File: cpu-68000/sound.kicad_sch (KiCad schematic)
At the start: 40 parts, among them U601 74HCT2G04, U602 SAA1099, U603 SAA1099, U604 LDL1117S50R, Y601 7.15909MHz

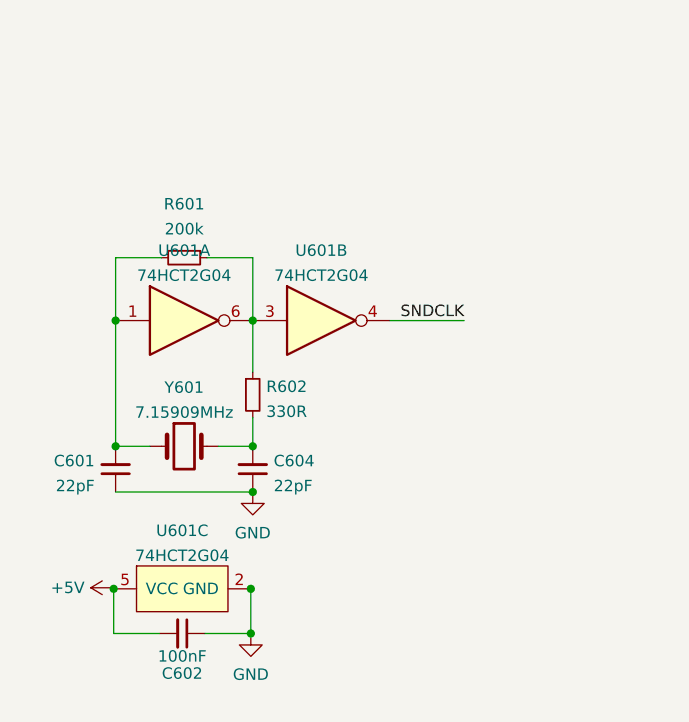
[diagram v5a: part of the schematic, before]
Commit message: Minor cleanup of CPU board
- Switched out of stock 2 bit level shifters for 8 bit part we already
  have; this means that the function codes will be buffered along with
  all other signals.
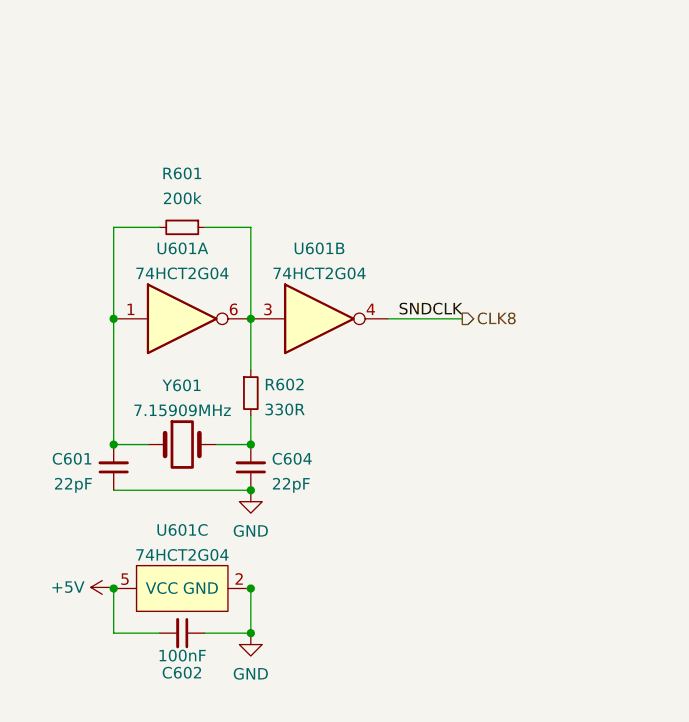
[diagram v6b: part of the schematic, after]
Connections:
- net SNDCLK renamed CLK8
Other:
- moved on the sheet: R601

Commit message: Major cleanup of CPU board
- A lot of traces got moved around to be less shitty

- Routed a few more signals to the GALs so that we can eliminate some
  discrete logic, namely for function code checking. This is critical
  since we need to reduce path length when switching the backplane bus
  buffers for each bus transaction as quick as possible.

- Actually provide a clock for the I2C master chip; it shares the clock
  with the audio chips, which is just a bit short of 8MHz.
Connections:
- net CLK8 renamed SNDCLK
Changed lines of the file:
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@@
     (effects (font (size 1.27 1.27)) (justify right))
   )
-  (hierarchical_label "CLK8" (shape output) (at 62.23 153.035 0)
+  (hierarchical_label "SNDCLK" (shape output) (at 62.23 153.035 0)
     (effects (font (size 1.27 1.27)) (justify left))
   )

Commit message: Schematic cleanup and ERC fixes
- Fixed many errors about duplicate or unassigned pins, and fixed some
  of the symbols and their pins directions.

- More minor tweaks to the pcb.
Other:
- company: (none) -> Tristan Seifert
- title: (none) -> 68komputer CPU Board
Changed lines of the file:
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@@
 (kicad_sch (version 20211123) (generator eeschema)
   (paper "A4")
+  (title_block
+    (title "68komputer CPU Board")
+    (date "2021-12-11")
+    (rev "1")
+    (company "Tristan Seifert")
+  )
   (junction (at 95.885 80.645) (diameter 0) (color 0 0 0 0)
   )
